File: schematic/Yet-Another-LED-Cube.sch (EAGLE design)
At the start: 7 parts, among them IC1 7805T, J1 DCJ0202

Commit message: added a bunch of parts
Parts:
- added IC2: MEGA48/88/168-PU, avr-6:MEGA48/88/168-PU
- added IC3, IC4: 74HC164N, 74xx-eu:74HC164N
- added Q1, Q10, Q11, Q12, Q13, Q14, Q15, Q16, Q2, Q3, Q4, Q5, Q6, Q7, Q8, Q9: 2N2907, transistor-pnp:2N2907
- added R1, R11, R13, R15, R17, R19, R21, R23, R25, R27, R29, R3, R31, R5, R7, R9: 1K, resistor:R-EU_0204/2V
- added R10, R12, R14, R16, R18, R2, R20, R22, R24, R26, R28, R30, R32, R33, R4, R6, R8: 10K, resistor:R-EU_0204/2V
- added U1: TLC5940-RHB, SparkFun:TLC5940-RHB
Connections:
- new net N$11: IC3A.QG, R5.1
- new net N$12: IC3A.QF, R3.1
- new net N$13: IC3A.QE, R1.1
- new net N$14: IC3A.QA, R9.1
- new net N$15: IC3A.QB, R11.1
- new net N$16: IC3A.QC, R13.1
- new net N$17: IC3A.QD, R15.1
- new net N$19: Q9.B, R17.2, R18.1
- new net N$2: Q1.B, R1.2, R2.1
- new net N$20: Q10.B, R19.2, R20.1
- new net N$21: Q11.B, R21.2, R22.1
- new net N$22: Q12.B, R23.2, R24.1
- new net N$23: Q13.B, R25.2, R26.1
- new net N$24: Q14.B, R27.2, R28.1
- new net N$25: Q15.B, R29.2, R30.1
- new net N$26: Q16.B, R31.2, R32.1
- new net N$27: IC4A.QH, R23.1
- new net N$28: IC4A.QG, R21.1
- new net N$29: IC4A.QF, R19.1
- new net N$3: Q2.B, R3.2, R4.1
- new net N$30: IC4A.QE, R17.1
- new net N$31: IC4A.QA, R25.1
- new net N$32: IC4A.QB, R27.1
- new net N$33: IC4A.QC, R29.1
- new net N$34: IC4A.QD, R31.1
- new net N$35: Q1.E, Q10.E, Q11.E, Q12.E, Q13.E, Q14.E, Q15.E, Q16.E, Q2.E, Q3.E, Q4.E, Q5.E, Q6.E, Q7.E, Q8.E, Q9.E, R10.2, R12.2, R14.2, R16.2, R18.2, R2.2, R20.2, R22.2, R24.2, R26.2, R28.2, R30.2, R32.2, R4.2, R6.2, R8.2
- new net N$36: IC3A.CLR, IC4A.CLR, R33.1
- new net N$37: IC3A.A, IC3A.B
- new net N$39: IC3A.CLK, IC4A.CLK
- new net N$4: Q3.B, R5.2, R6.1
- new net N$40: IC3A.QH, IC4A.A, IC4A.B, R7.1
- new net N$5: Q4.B, R7.2, R8.1
- new net N$6: Q5.B, R10.1, R9.2
- new net N$7: Q6.B, R11.2, R12.1
- new net N$8: Q7.B, R13.2, R14.1
- new net N$9: Q8.B, R15.2, R16.1
- net +5V: now also R33.2
- net GND: now also IC1.GND
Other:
- moved on the sheet: C1, C2, C3, C4, IC1, J1, S1

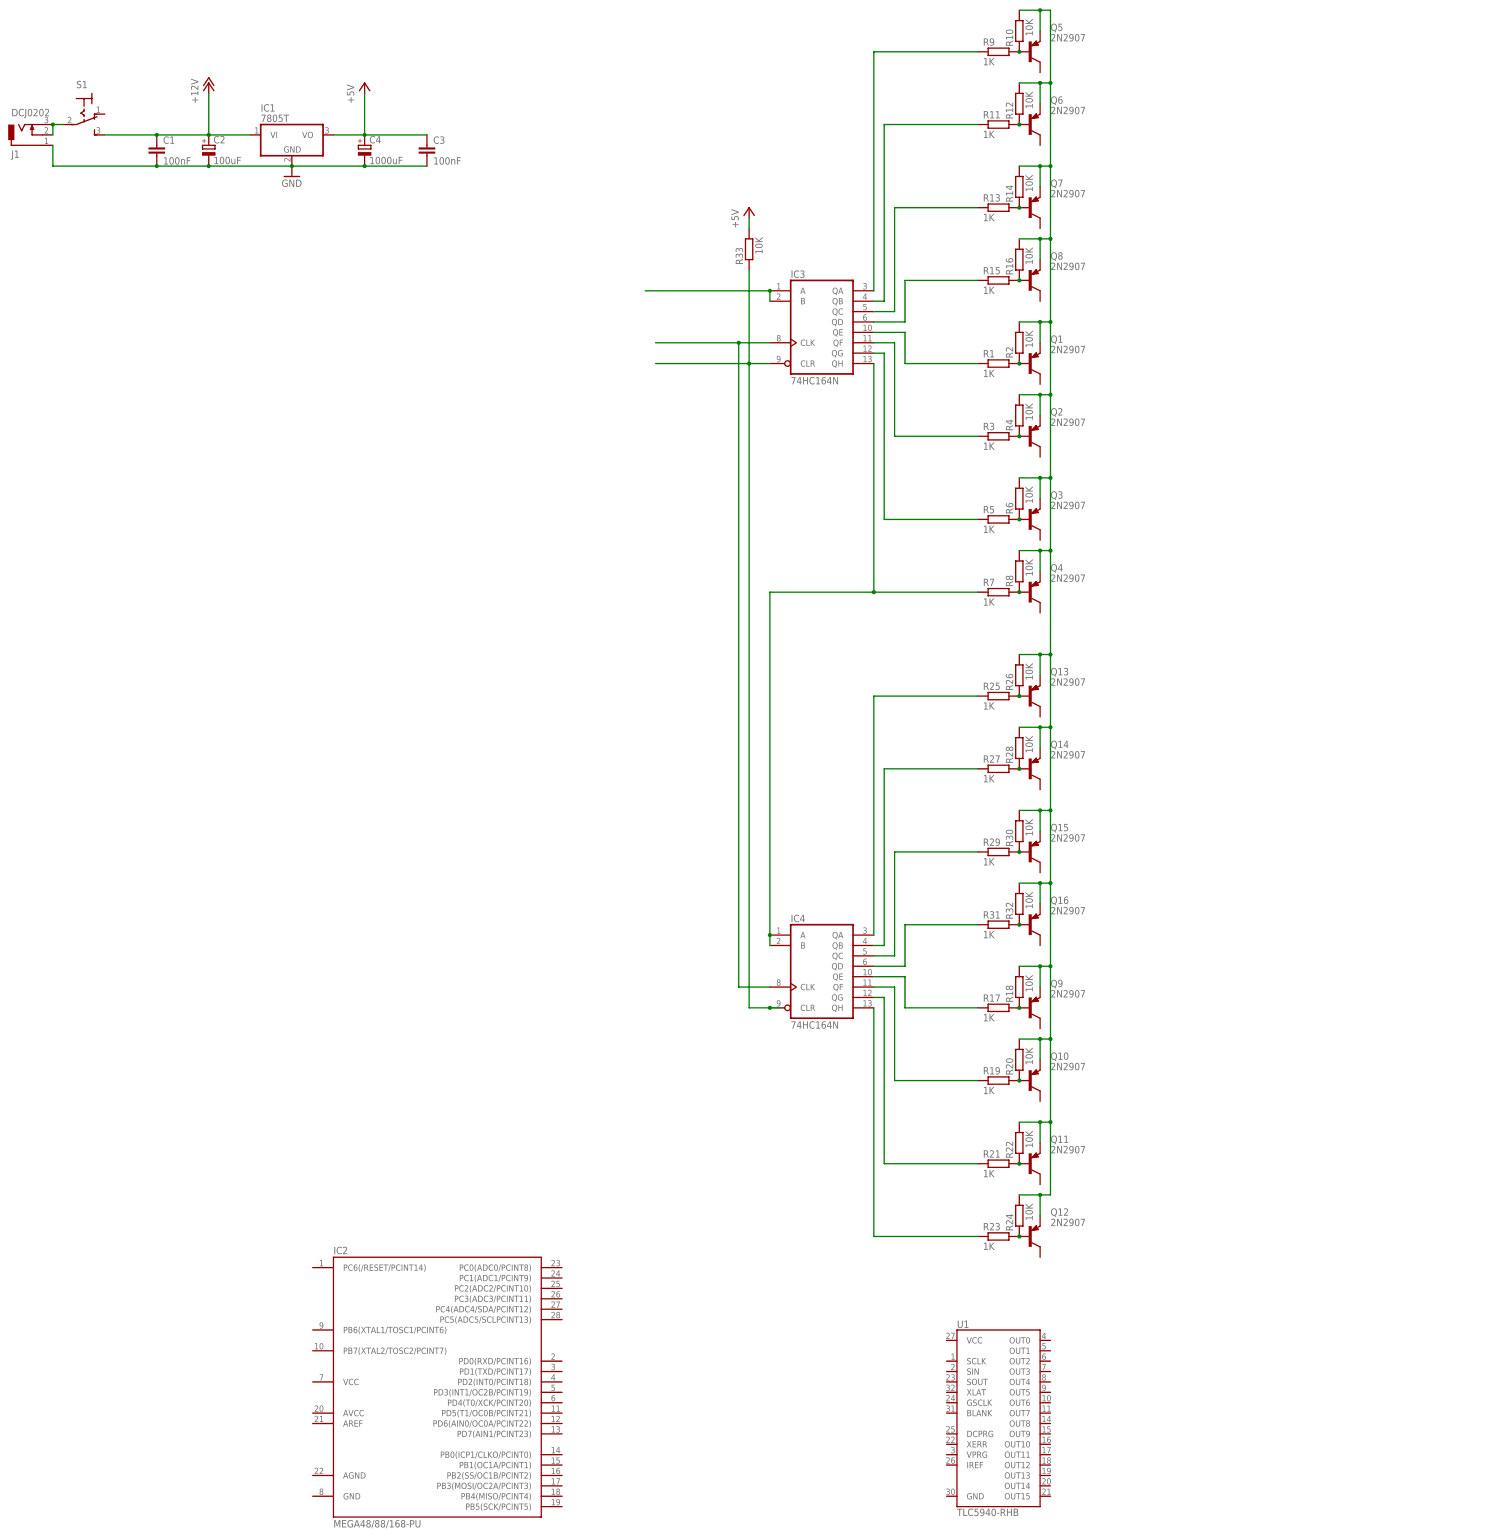
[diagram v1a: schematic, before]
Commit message: Add RGB LED parts; connect IC's
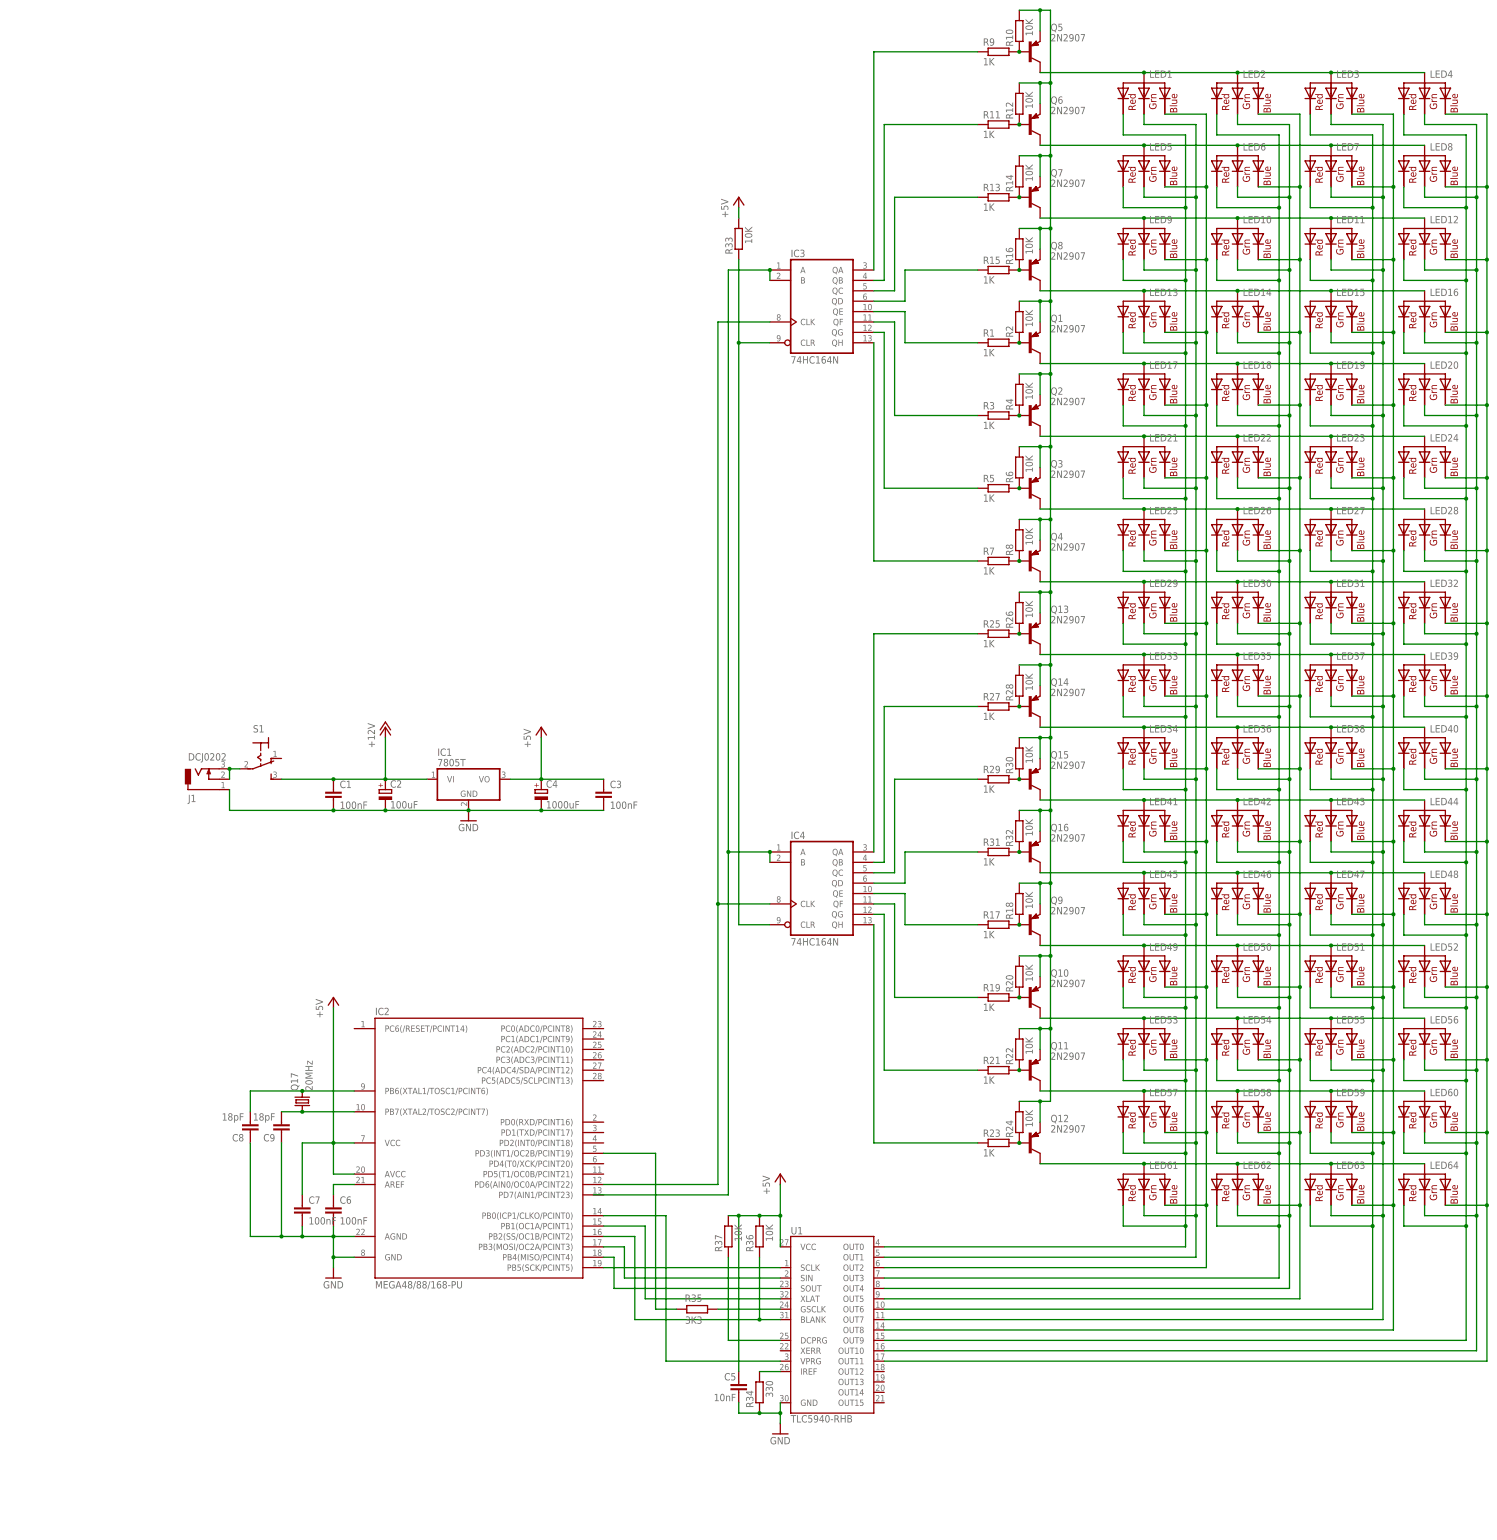
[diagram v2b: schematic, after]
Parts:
- added C5: 10nF, rcl:C-EU025-024X044
- added C6, C7: 100nF, rcl:C-EU025-024X044
- added C8, C9: 18pF, rcl:C-EU025-024X044
- added LED1, LED10, LED11, LED12, LED13, LED14, LED15, LED16, LED17, LED18, LED19, LED2, LED20, LED21, LED22, LED23, LED24, LED25, LED26, LED27, LED28, LED29, LED3, LED30, LED31, LED32, LED33, LED34, LED35, LED36, LED37, LED38, LED39, LED4, LED40, LED41, LED42, LED43, LED44, LED45, LED46, LED47, LED48, LED49, LED5, LED50, LED51, LED52, LED53, LED54, LED55, LED56, LED57, LED58, LED59, LED6, LED60, LED61, LED62, LED63, LED64, LED7, LED8, LED9: RGBLED_CAA, adafruit:RGBLED_CAA
- added Q17: 20MHz, crystal:CRYSTALHC49S
- added R34: 330, resistor:R-EU_0204/2V
- added R35: 3K3, resistor:R-EU_0204/2V
- added R36, R37: 10K, resistor:R-EU_0204/2V
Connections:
- removed net N$40 (its old number): IC3A.QH, IC4A.A, IC4A.B, R7.1
- new net N$10: LED1.RED, LED13.RED, LED17.RED, LED21.RED, LED25.RED, LED29.RED, LED33.RED, LED34.RED, LED41.RED, LED45.RED, LED49.RED, LED5.RED, LED53.RED, LED57.RED, LED61.RED, LED9.RED, U1.OUT0
- new net N$124: LED29.VCC, LED30.VCC, LED31.VCC, LED32.VCC, Q4.C
- new net N$125: LED25.VCC, LED26.VCC, LED27.VCC, LED28.VCC, Q3.C
- new net N$126: LED21.VCC, LED22.VCC, LED23.VCC, LED24.VCC, Q2.C
- new net N$127: LED17.VCC, LED18.VCC, LED19.VCC, LED20.VCC, Q1.C
- new net N$128: LED13.VCC, LED14.VCC, LED15.VCC, LED16.VCC, Q8.C
- new net N$129: LED10.VCC, LED11.VCC, LED12.VCC, LED9.VCC, Q7.C
- new net N$18: LED1.GREEN, LED13.GREEN, LED17.GREEN, LED21.GREEN, LED25.GREEN, LED29.GREEN, LED33.GREEN, LED34.GREEN, LED41.GREEN, LED45.GREEN, LED49.GREEN, LED5.GREEN, LED53.GREEN, LED57.GREEN, LED61.GREEN, LED9.GREEN, U1.OUT1
- new net N$34: IC2.PB5(SCK/PCINT5), U1.SCLK
- new net N$35: LED1.VCC, LED2.VCC, LED3.VCC, LED4.VCC, Q5.C
- new net N$36: IC2.PD6(AIN0/OC0A/PCINT22), IC3A.CLK, IC4A.CLK
- new net N$38: LED1.BLUE, LED13.BLUE, LED17.BLUE, LED21.BLUE, LED25.BLUE, LED29.BLUE, LED33.BLUE, LED34.BLUE, LED41.BLUE, LED45.BLUE, LED49.BLUE, LED5.BLUE, LED53.BLUE, LED57.BLUE, LED61.BLUE, LED9.BLUE, U1.OUT2
- new net N$41: LED5.VCC, LED6.VCC, LED7.VCC, LED8.VCC, Q6.C
- new net N$42: LED10.RED, LED14.RED, LED18.RED, LED2.RED, LED22.RED, LED26.RED, LED30.RED, LED35.RED, LED36.RED, LED42.RED, LED46.RED, LED50.RED, LED54.RED, LED58.RED, LED6.RED, LED62.RED, U1.OUT3
- new net N$43: LED10.GREEN, LED14.GREEN, LED18.GREEN, LED2.GREEN, LED22.GREEN, LED26.GREEN, LED30.GREEN, LED35.GREEN, LED36.GREEN, LED42.GREEN, LED46.GREEN, LED50.GREEN, LED54.GREEN, LED58.GREEN, LED6.GREEN, LED62.GREEN, U1.OUT4
- new net N$44: LED10.BLUE, LED14.BLUE, LED18.BLUE, LED2.BLUE, LED22.BLUE, LED26.BLUE, LED30.BLUE, LED35.BLUE, LED36.BLUE, LED42.BLUE, LED46.BLUE, LED50.BLUE, LED54.BLUE, LED58.BLUE, LED6.BLUE, LED62.BLUE, U1.OUT5
- new net N$45: IC3A.QH, R7.1
- new net N$46: LED11.RED, LED15.RED, LED19.RED, LED23.RED, LED27.RED, LED3.RED, LED31.RED, LED37.RED, LED38.RED, LED43.RED, LED47.RED, LED51.RED, LED55.RED, LED59.RED, LED63.RED, LED7.RED, U1.OUT6
- new net N$47: LED11.GREEN, LED15.GREEN, LED19.GREEN, LED23.GREEN, LED27.GREEN, LED3.GREEN, LED31.GREEN, LED37.GREEN, LED38.GREEN, LED43.GREEN, LED47.GREEN, LED51.GREEN, LED55.GREEN, LED59.GREEN, LED63.GREEN, LED7.GREEN, U1.OUT7
- new net N$48: LED11.BLUE, LED15.BLUE, LED19.BLUE, LED23.BLUE, LED27.BLUE, LED3.BLUE, LED31.BLUE, LED37.BLUE, LED38.BLUE, LED43.BLUE, LED47.BLUE, LED51.BLUE, LED55.BLUE, LED59.BLUE, LED63.BLUE, LED7.BLUE, U1.OUT8
- new net N$49: IC2.PB4(MISO/PCINT4), U1.SOUT
- new net N$50: LED12.RED, LED16.RED, LED20.RED, LED24.RED, LED28.RED, LED32.RED, LED39.RED, LED4.RED, LED40.RED, LED44.RED, LED48.RED, LED52.RED, LED56.RED, LED60.RED, LED64.RED, LED8.RED, U1.OUT9
- new net N$51: LED12.GREEN, LED16.GREEN, LED20.GREEN, LED24.GREEN, LED28.GREEN, LED32.GREEN, LED39.GREEN, LED4.GREEN, LED40.GREEN, LED44.GREEN, LED48.GREEN, LED52.GREEN, LED56.GREEN, LED60.GREEN, LED64.GREEN, LED8.GREEN, U1.OUT10
- new net N$52: LED12.BLUE, LED16.BLUE, LED20.BLUE, LED24.BLUE, LED28.BLUE, LED32.BLUE, LED39.BLUE, LED4.BLUE, LED40.BLUE, LED44.BLUE, LED48.BLUE, LED52.BLUE, LED56.BLUE, LED60.BLUE, LED64.BLUE, LED8.BLUE, U1.OUT11
- new net N$54: IC2.PB1(OC1A/PCINT1), U1.XLAT
- new net N$55: IC2.PD3(INT1/OC2B/PCINT19), R35.2
- new net N$56: IC2.PB2(SS/OC1B/PCINT2), R36.1, U1.BLANK
- new net N$57: IC2.PB0(ICP1/CLKO/PCINT0), U1.VPRG
- new net N$58: R34.2, U1.IREF
- new net N$59: R35.1, U1.GSCLK
- new net N$60: R37.1, U1.DCPRG
- new net N$61: LED33.VCC, LED35.VCC, LED37.VCC, LED39.VCC, Q13.C
- new net N$62: LED34.VCC, LED36.VCC, LED38.VCC, LED40.VCC, Q14.C
- new net N$63: LED61.VCC, LED62.VCC, LED63.VCC, LED64.VCC, Q12.C
- new net N$64: LED57.VCC, LED58.VCC, LED59.VCC, LED60.VCC, Q11.C
- new net N$65: LED53.VCC, LED54.VCC, LED55.VCC, LED56.VCC, Q10.C
- new net N$66: LED49.VCC, LED50.VCC, LED51.VCC, LED52.VCC, Q9.C
- new net N$67: LED45.VCC, LED46.VCC, LED47.VCC, LED48.VCC, Q16.C
- new net N$68: LED41.VCC, LED42.VCC, LED43.VCC, LED44.VCC, Q15.C
- new net N$70: C6.1, IC2.AREF
- new net N$72: C8.2, IC2.PB6(XTAL1/TOSC1/PCINT6), Q17.2
- new net N$73: C9.2, IC2.PB7(XTAL2/TOSC2/PCINT7), Q17.1
- net +5V: now also C5.1, C7.1, IC2.AVCC, IC2.VCC@1, R36.2, R37.2, U1.VCC
- net GND: now also C5.2, C6.2, C7.2, C8.1, C9.1, IC2.AGND, IC2.GND@1, R34.1, U1.GND
- net N$37: now also IC4A.A, IC4A.B
- net N$39: now also IC2.PB3(MOSI/OC2A/PCINT3), U1.SIN; no longer IC3A.CLK, IC4A.CLK
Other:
- moved on the sheet: C1, C2, C3, C4, IC1, IC2, IC3, IC4, J1, Q1, Q10, Q11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
